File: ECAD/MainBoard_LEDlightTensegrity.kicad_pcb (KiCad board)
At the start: 2 copper layers, 85 x 30 mm, 15 parts, among them IC1 ARDUINO_PRO_MINI_5V, K1 CONN_3, K2 CONN_3, K3 CONN_3, P1 CONN_2, P2 CONN_2, SW1 SPST, U1 OKL-T6-W12, U2 CJ1117-3.3, U3 REDBOTACCEL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

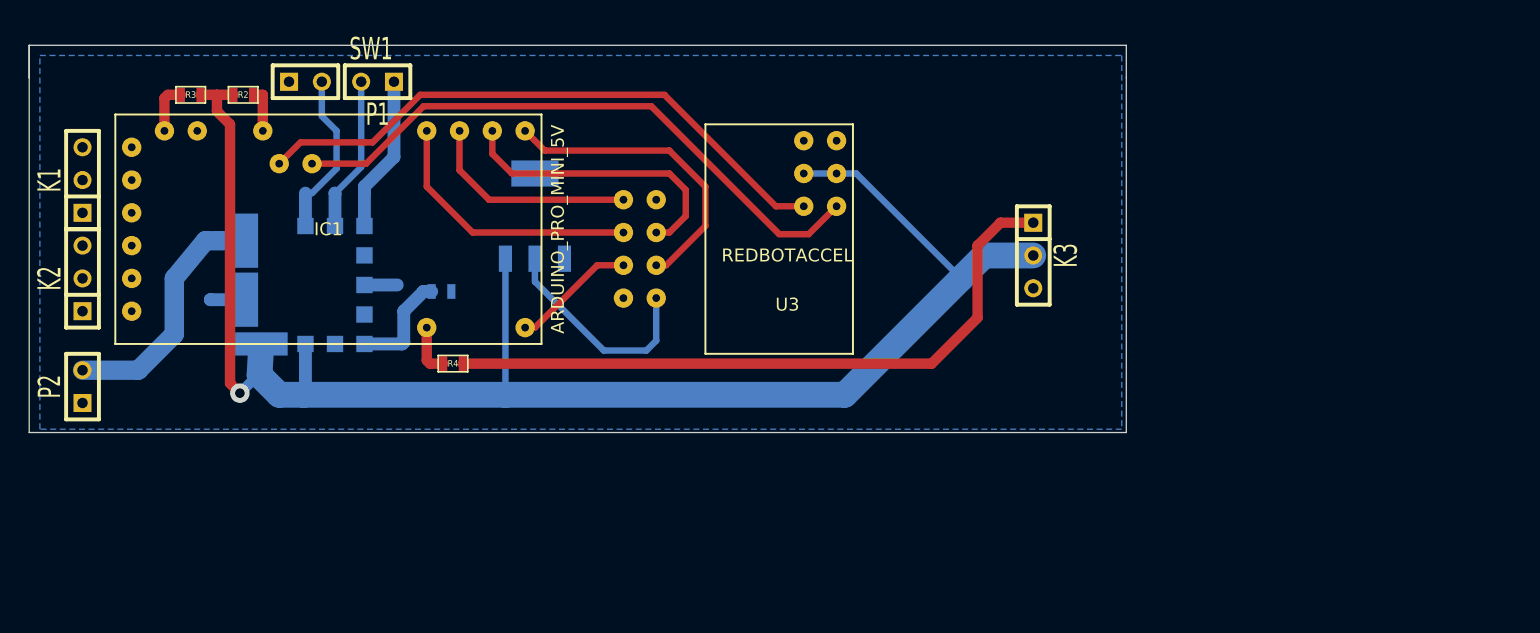
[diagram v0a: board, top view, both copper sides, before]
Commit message: Added Protection Diode and Secondary Battery Path
Added Reverse Voltage Protection Diode. Also added second battery input
if only two batteries are used vs 4 total (2x on each side). Added
footprint for diode DO-214AB
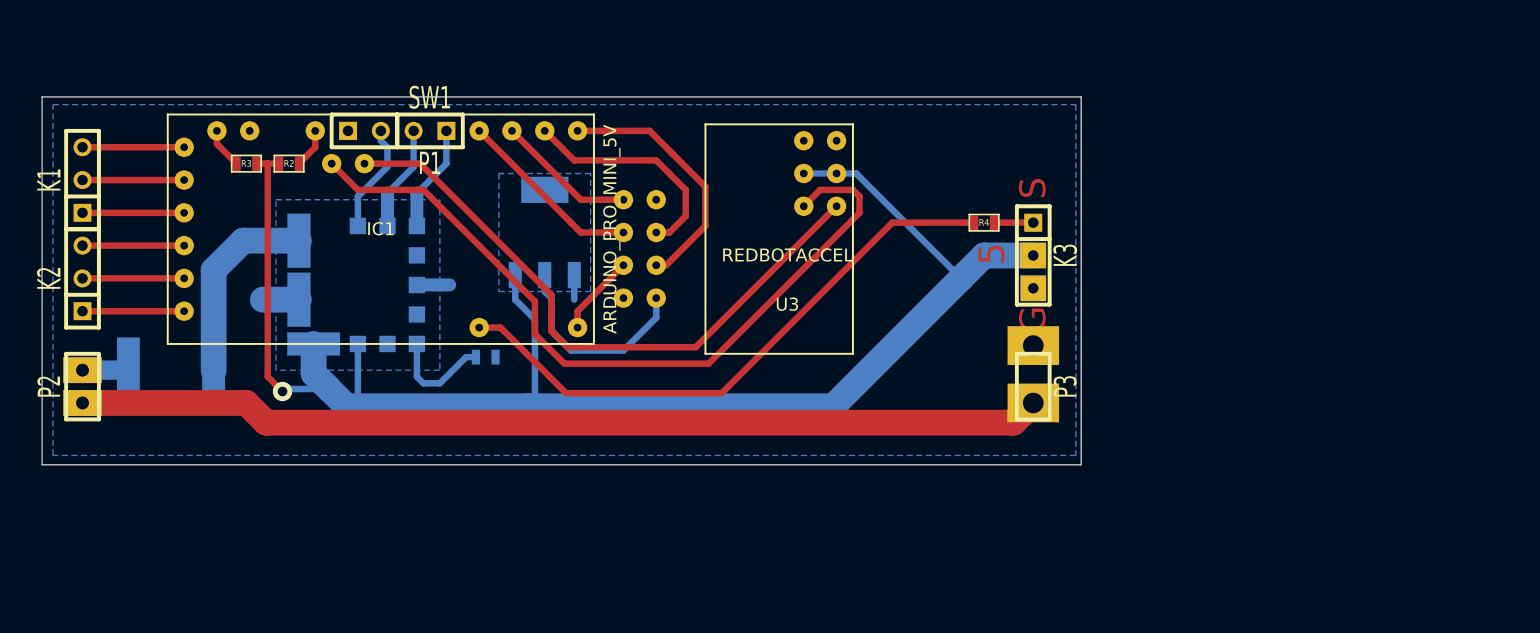
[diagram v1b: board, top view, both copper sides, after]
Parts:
- added D1: DIODE, DO-214AB(HSMC), B.Cu at (31.0, 42.7)
- added P3: CONN_2, SIL-2, F.Cu at (97.8, 43.9)
- IC1: footprint ArduinoProMini-5V -> ArduinoProMini-5V-reduced
- moved R4 42.6 mm to (94.0, 31.2)
- moved R3 6.86 mm to (36.8, 26.7)
- moved R2 6.41 mm to (40.1, 26.7)
- moved R1 6.13 mm to (55.4, 41.7)
- moved SW1 5.95 mm to (46.0, 24.1)
- moved P1 5.57 mm to (51.1, 24.1)
- moved IC1 4.06 mm to (47.2, 31.8)
- moved U1 4.06 mm to (45.5, 36.1)
- moved U2 1.48 mm to (59.9, 32.0)
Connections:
- P2 pad 1: GND -> VAA
- U1 pad 2: VCC -> N-0000031
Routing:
- net VAA: track 0.00 -> 74.9 mm
- net /LED: track 52.0 -> 3.05 mm
- net N-000005: track 3.92 -> 45.9 mm
- net VCC: track 19.6 -> 3.56 mm
- net N-0000031: track 0.00 -> 15.3 mm
- net /SCL: track 46.4 -> 60.0 mm
- net N-0000048: track 0.00 -> 7.87 mm
- net N-0000042: track 0.00 -> 7.87 mm
- net N-0000026: track 0.00 -> 7.87 mm
- net N-0000025: track 0.00 -> 7.87 mm
- net N-0000024: track 0.00 -> 7.87 mm
- net N-0000023: track 0.00 -> 7.87 mm
- net +5V: track 128.3 -> 120.7 mm
- net /SCK: track 21.0 -> 14.4 mm
- net /MISO: track 16.7 -> 10.8 mm
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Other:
- board size 85 x 30 mm -> 80.5 x 28.5 mm
- board text added: "5"
- board text added: "G"
- board text added: "S"

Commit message: Added updated Gerbers
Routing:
- net GND: track 7.24 -> 15.8 mm
- net +5V: track 120.7 -> 117.2 mm
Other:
- net class Default: trace_width 0.5 -> 2
- board text added: "+"
- board text added: "-"
- board text added: "ACCEL"
- board text added: "Battery"
- board text added: "LEDlightTensegrity v1"
- board text added: "colinho"
- board text added: "nRF24L01+"
- board text removed: "G"
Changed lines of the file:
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@@
     (links 42)
     (no_connects 0)
-    (area 20.949999 21.449999 101.550001 48.050001)
+    (area 9.000001 20.31873 101.63175 50.050001)
     (thickness 1.6)
-    (drawings 8)
-    (tracks 119)
+    (drawings 19)
+    (tracks 124)
     (zones 0)
     (modules 17)
@@
   (layers
     (15 F.Cu signal)
-    (0 B.Cu signal)
+    (0 B.Cu signal hide)
     (16 B.Adhes user)
     (17 F.Adhes user)
@@
   )
   (setup
-    (last_trace_width 0.5)
+    (last_trace_width 2)
     (trace_clearance 0.254)
     (zone_clearance 0.508)
@@
     (mod_text_size 1 1)
     (mod_text_width 0.15)
-    (pad_size 3 4)
-    (pad_drill 1.6)
+    (pad_size 2 5)
+    (pad_drill 0.8128)
     (pad_to_mask_clearance 0)
     (aux_axis_origin 0 0)
@@
   (net_class Default "This is the default net class."
     (clearance 0.254)
-    (trace_width 0.5)
+    (trace_width 2)
     (via_dia 1.5)
     (via_drill 0.85)
@@
       (net 4 /LED)
     )
-    (pad 2 thru_hole rect (at 0 0 270) (size 2 2) (drill 0.8128)
+    (pad 2 thru_hole rect (at 0 1.27 270) (size 2 5) (drill 0.8128)
       (layers *.Cu *.Mask F.SilkS)
       (net 1 +5V)
     )
-    (pad 3 thru_hole rect (at 2.54 0 270) (size 2 2) (drill 0.8128)
+    (pad 3 thru_hole rect (at 2.54 1.397 270) (size 2 5) (drill 0.8128)
       (layers *.Cu *.Mask F.SilkS)
       (net 10 GND)
@@
     )
   )
+  (gr_text nRF24L01+ (at 71.628 32.893 90) (layer B.Cu)
+    (effects (font (size 1 1) (thickness 0.25)) (justify mirror))
+  )
+  (dimension 80.5 (width 0.3) (layer Edge.Cuts)
+    (gr_text "80.500 mm" (at 61.25 55.349999) (layer Edge.Cuts)
+      (effects (font (size 1.5 1.5) (thickness 0.3)))
+    )
+    (feature1 (pts (xy 21 50) (xy 21 56.699999)))
+    (feature2 (pts (xy 101.5 50) (xy 101.5 56.699999)))
+    (crossbar (pts (xy 101.5 53.999999) (xy 21 53.999999)))
+    (arrow1a (pts (xy 21 53.999999) (xy 22.126503 53.413579)))
+    (arrow1b (pts (xy 21 53.999999) (xy 22.126503 54.586419)))
+    (arrow2a (pts (xy 101.5 53.999999) (xy 100.373497 53.413579)))
+    (arrow2b (pts (xy 101.5 53.999999) (xy 100.373497 54.586419)))
+  )
+  (gr_text "ACCEL\n" (at 77.216 27.686 90) (layer F.Cu)
+    (effects (font (size 1 1) (thickness 0.25)))
+  )
+  (gr_text Battery (at 29.21 47.752) (layer F.Cu)
+    (effects (font (size 1 1) (thickness 0.25)))
+  )
+  (gr_text colinho (at 97.663 25.781) (layer F.Cu)
+    (effects (font (size 1 1) (thickness 0.25)))
+  )
+  (gr_text "LEDlightTensegrity v1" (at 92.329 23.876) (layer F.Cu)
+    (effects (font (size 1 1) (thickness 0.25)))
+  )
+  (gr_text "-\n" (at 24.13 47.752 180) (layer F.Cu)
+    (effects (font (size 2 2) (thickness 0.5)))
+  )
+  (gr_text + (at 27.305 42.418 90) (layer F.Cu)
+    (effects (font (size 2 2) (thickness 0.5)))
+  )
+  (gr_text Battery (at 91.186 42.164 90) (layer F.Cu)
+    (effects (font (size 1 1) (thickness 0.25)))
+  )
+  (gr_text "-\n" (at 94.615 36.449 90) (layer F.Cu)
+    (effects (font (size 2 2) (thickness 0.5)))
+  )
+  (gr_text + (at 93.472 44.323 90) (layer F.Cu)
+    (effects (font (size 2 2) (thickness 0.5)))
+  )
+  (gr_text "-\n" (at 93.472 40.64 90) (layer F.Cu)
+    (effects (font (size 2 2) (thickness 0.5)))
+  )
   (dimension 28.5 (width 0.3) (layer Edge.Cuts)
     (gr_text "28.500 mm" (at 15.65 35.75 90) (layer Edge.Cuts)
@@
     (effects (font (size 2 2) (thickness 0.5)))
   )
-  (gr_text G (at 97.79 38.735 90) (layer F.Cu)
-    (effects (font (size 2 2) (thickness 0.5)))
-  )
+  (segment (start 82.55 27.432) (end 84.201 27.432) (width 0.5) (layer B.Cu) (net 1) (status 400000))
+  (segment (start 84.328 27.432) (end 90.678 33.782) (width 0.5) (layer B.Cu) (net 1))
+  (segment (start 84.201 27.432) (end 84.328 27.432) (width 0.5) (layer B.Cu) (net 1))
+  (segment (start 96.52 33.782) (end 90.678 33.782) (width 2) (layer B.Cu) (net 1) (status 400000))
+  (segment (start 90.678 33.782) (end 87.376 33.782) (width 2) (layer B.Cu) (net 1))
+  (segment (start 73.025 45.466) (end 58.674 45.466) (width 2) (layer B.Cu) (net 1))
+  (segment (start 75.692 45.466) (end 87.376 33.782) (width 2) (layer B.Cu) (net 1))
+  (segment (start 75.184 45.466) (end 75.692 45.466) (width 2) (layer B.Cu) (net 1))
+  (segment (start 73.025 45.466) (end 75.184 45.466) (width 2) (layer B.Cu) (net 1))
   (segment (start 57.658 35.306) (end 57.658 37.211) (width 0.5) (layer B.Cu) (net 1))
   (segment (start 59.182 44.958) (end 58.674 45.466) (width 0.5) (layer B.Cu) (net 1))
@@
   (segment (start 42.036 40.638) (end 42.036 42.926) (width 2) (layer B.Cu) (net 1))
   (segment (start 42.037 42.926) (end 43.2435 44.1325) (width 2) (layer B.Cu) (net 1))
-  (segment (start 82.296 45.466) (end 92.202 35.56) (width 2) (layer B.Cu) (net 1))
   (segment (start 42.799 43.688) (end 44.577 45.466) (width 2) (layer B.Cu) (net 1))
   (segment (start 43.2435 44.1325) (end 42.799 43.688) (width 2) (layer B.Cu) (net 1))
   (segment (start 44.577 45.466) (end 58.674 45.466) (width 2) (layer B.Cu) (net 1))
-  (segment (start 58.674 45.466) (end 82.296 45.466) (width 2) (layer B.Cu) (net 1))
   (segment (start 45.466 40.638) (end 45.466 45.72) (width 0.5) (layer B.Cu) (net 1))
   (segment (start 37.592 26.67) (end 38.481 26.67) (width 0.5) (layer F.Cu) (net 1))
@@
   (segment (start 38.354 26.67) (end 39.37 26.67) (width 0.5) (layer F.Cu) (net 1))
   (segment (start 80.01 27.432) (end 82.55 27.432) (width 0.5) (layer B.Cu) (net 1))
-  (segment (start 82.55 27.432) (end 84.074 27.432) (width 0.5) (layer B.Cu) (net 1))
-  (segment (start 84.074 27.432) (end 92.202 35.56) (width 0.5) (layer B.Cu) (net 1))
-  (segment (start 92.202 35.56) (end 93.98 33.782) (width 2) (layer B.Cu) (net 1))
-  (segment (start 93.98 33.782) (end 97.79 33.782) (width 2) (layer B.Cu) (net 1))
   (segment (start 66.04 34.544) (end 62.484 38.1) (width 0.5) (layer F.Cu) (net 2))
   (segment (start 62.484 38.1) (end 62.484 39.37) (width 0.5) (layer F.Cu) (net 2))
@@
   (segment (start 71.628 40.894) (end 61.722 40.894) (width 0.5) (layer F.Cu) (net 9))
   (segment (start 73.152 39.37) (end 71.628 40.894) (width 0.5) (layer F.Cu) (net 9))
-  (segment (start 62.23 35.306) (end 62.23 37.211) (width 0.5) (layer B.Cu) (net 10) (status 400000))
+  (segment (start 96.393 36.322) (end 92.202 36.322) (width 2) (layer B.Cu) (net 10) (status 400000))
+  (segment (start 97.79 40.767) (end 93.472 40.767) (width 2) (layer B.Cu) (net 10))
+  (segment (start 62.23 35.306) (end 62.23 37.211) (width 0.5) (layer B.Cu) (net 10))
   (segment (start 40.896 37.208) (end 38.103 37.208) (width 2) (layer B.Cu) (net 10))
   (segment (start 38.103 37.208) (end 38.1 37.211) (width 1) (layer B.Cu) (net 10))

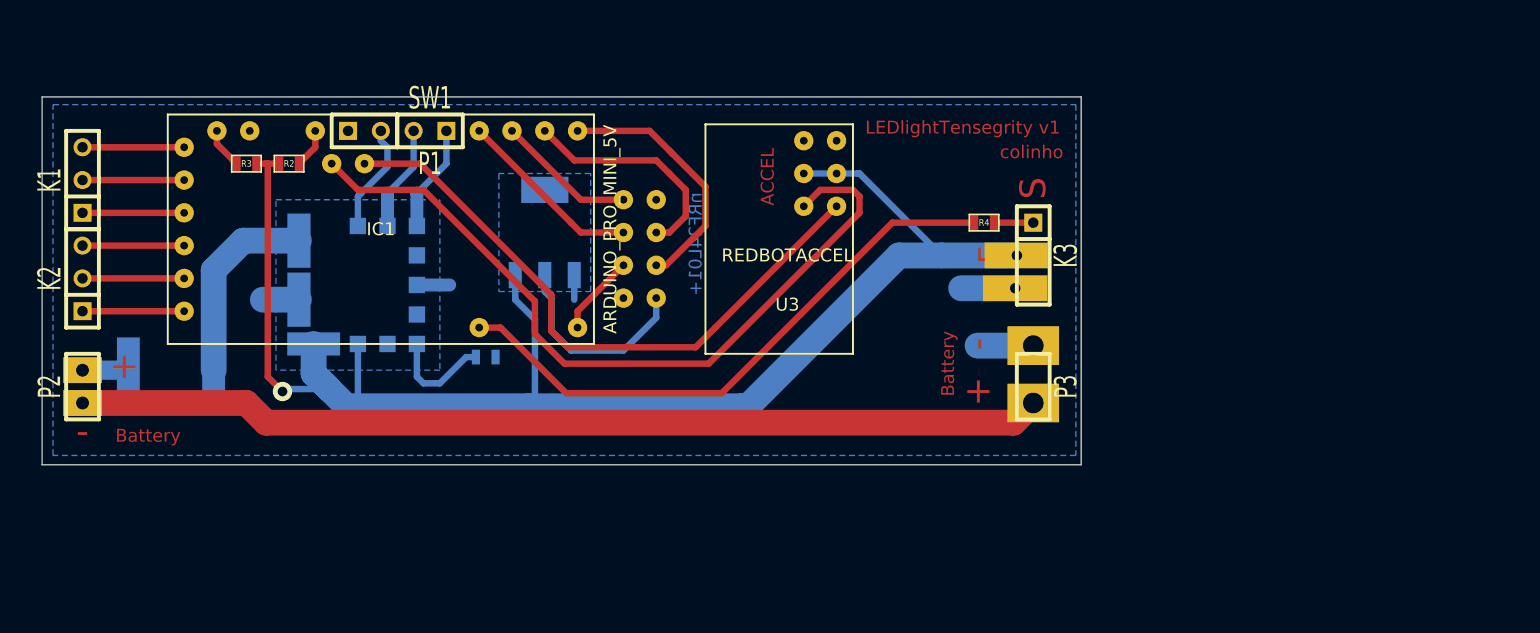
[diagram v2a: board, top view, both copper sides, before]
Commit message: Changed drills to sizes for LPKF board mill
LPKF board mill doesn't have 0.85mm drill, KiCAD vias are 0.85mm
standard. Drove me crazy trying to find it...
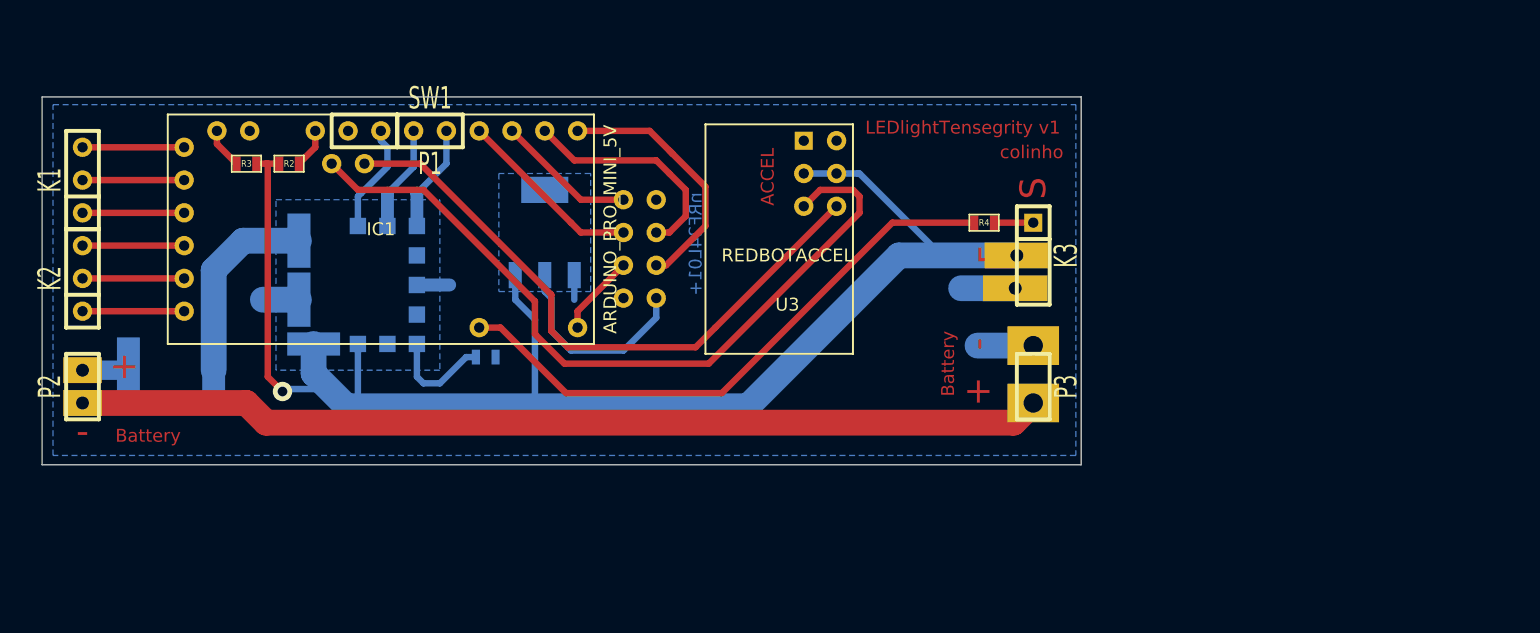
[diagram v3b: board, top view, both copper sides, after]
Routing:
- net +5V: track 117.2 -> 177.5 mm
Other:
- net class Default: via_drill 0.85 -> 0.8

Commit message: Changed outer cut for structural mounting
Extended board cuts so it can be mounted to 3D printed brackets
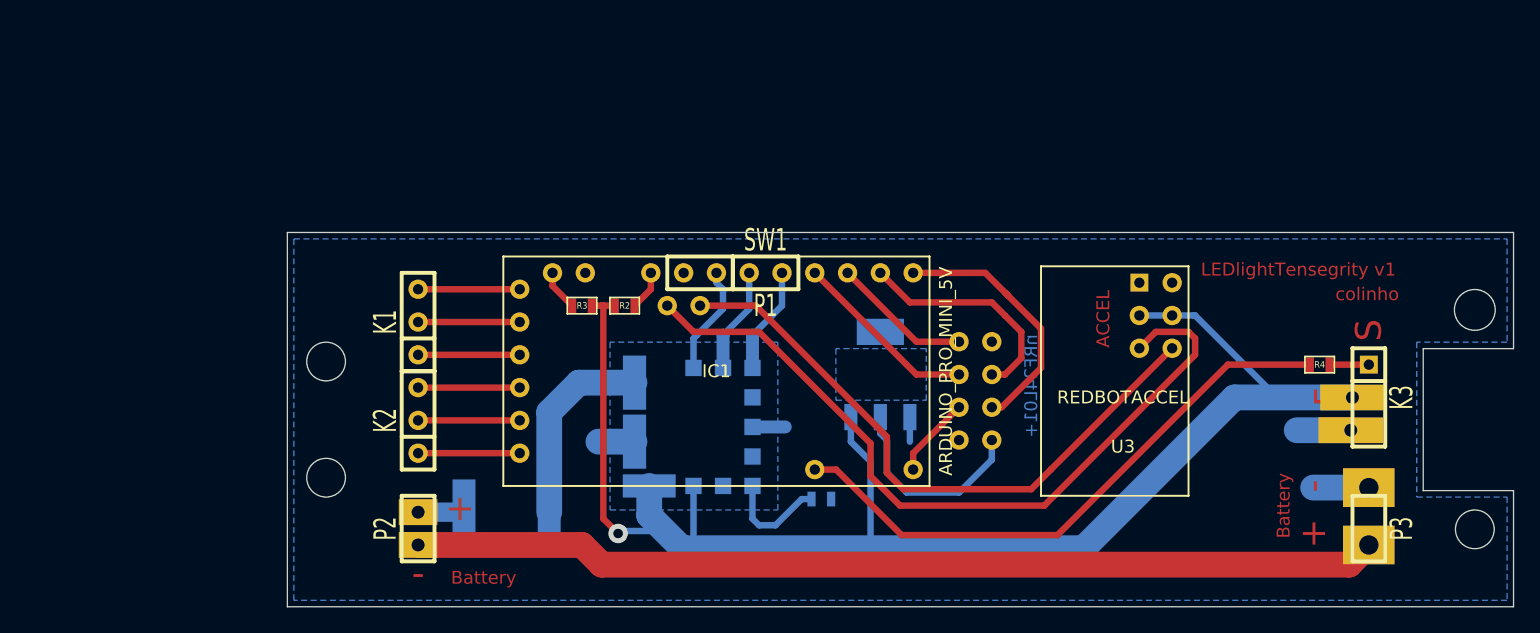
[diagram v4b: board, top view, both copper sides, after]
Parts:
- moved SW1 28.2 mm to (72.0, 35.1)
- moved D1 28.2 mm to (57.0, 53.7)
- moved IC1 28.2 mm to (73.2, 42.8)
- moved K3 28.2 mm to (123.8, 44.8)
- moved P1 28.2 mm to (77.1, 35.1)
- moved P3 28.2 mm to (123.8, 54.9)
- moved R1 28.2 mm to (81.4, 52.7)
- moved R2 28.2 mm to (66.1, 37.7)
- moved R3 28.2 mm to (62.8, 37.7)
- moved U2 28.2 mm to (85.9, 43.0)
- moved U3 28.2 mm to (108.5, 35.9)
- moved U4 28.2 mm to (92.0, 48.1)
- moved K1 28.2 mm to (50.1, 38.9)
- moved K2 28.2 mm to (50.1, 46.6)
- moved P2 28.2 mm to (50.1, 54.9)
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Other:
- board size 80.5 x 28.5 mm -> 95 x 29 mm
